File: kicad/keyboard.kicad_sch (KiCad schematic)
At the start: 64 parts

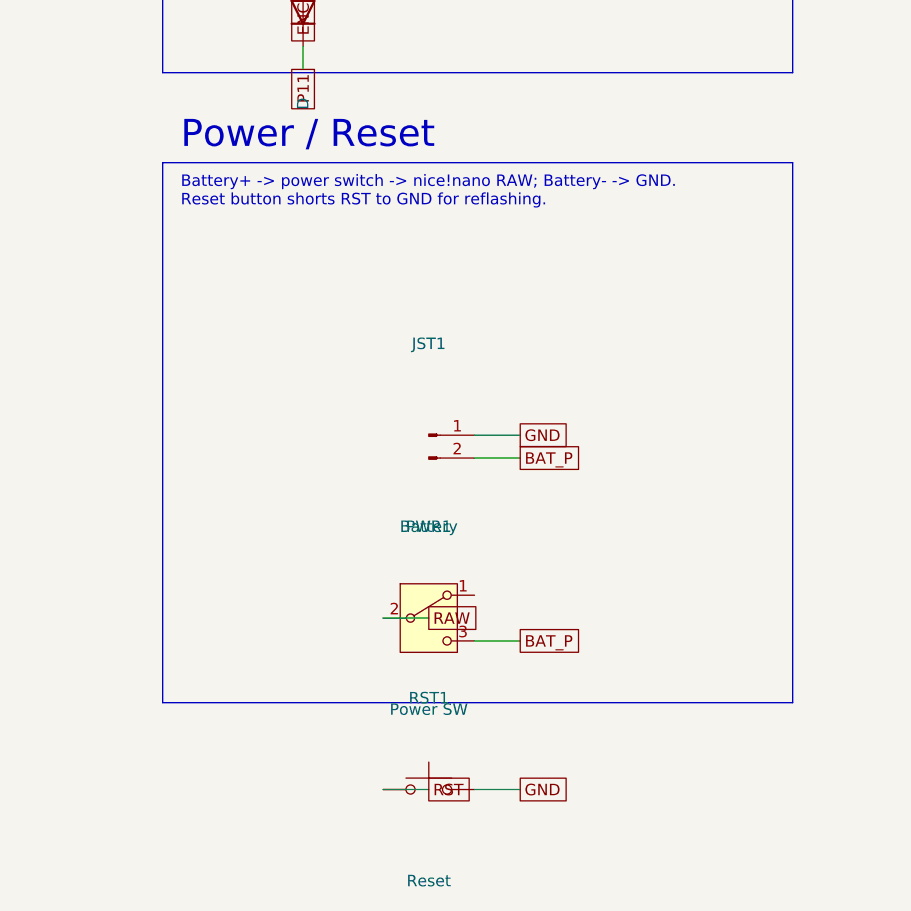
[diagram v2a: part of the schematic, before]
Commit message: Use Typeractive reset button (Panasonic EVQ-PUC02K, SMD side)
- Switch reset from reset_switch_tht_top to ceoloide/reset_switch_smd_side,
  which matches the Typeractive reset button (Panasonic EVQ-PUC02K). The
  power switch was already the matching part (Alps SSSS811101 =
  power_switch_smd_side), so it is unchanged.
- Vendor reset_switch_smd_side.js footprint
- Wiring verified: RST1 -> {GND, RST}; PWR1 -> {BAT_P, RAW}; matrix intact
- Schematic: map the new footprint, lay Power/Reset parts side-by-side so
  pin labels don't collide (fixes a schematic-only net short); netlist clean
- Regenerate output/ and KiCad project
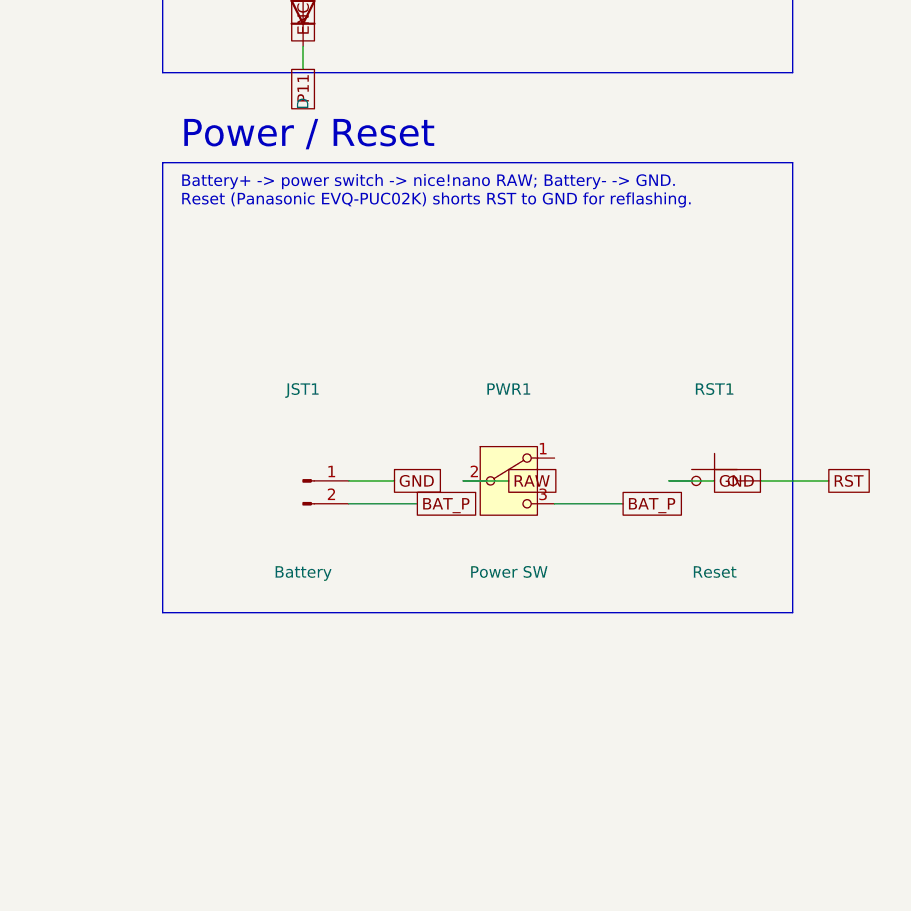
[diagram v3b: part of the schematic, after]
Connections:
- net GND: now also RST1.1; no longer RST1.2
- net RST: now also RST1.2; no longer RST1.1
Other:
- note added: "Battery+ -> power switch -> nice!nano RAW; Battery- -> GND. Reset (Panasonic EVQ-PUC02K) shorts RST to GND for reflashing."
- note removed: "Battery+ -> power switch -> nice!nano RAW; Battery- -> GND. Reset button shorts RST to GND for reflashing."
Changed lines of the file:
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@@
   (global_label "P11" (shape passive) (at 261.62 167.64 270)
     (effects (font (size 1.27 1.27)) (justify right)))
-  (rectangle (start 246.02 178.00) (end 316.02 238.00)
+  (rectangle (start 246.02 178.00) (end 316.02 228.00)
     (stroke (width 0.15) (type solid)) (fill (type none)))
   (text "Power / Reset" (at 248.02 175.00 0)
     (effects (font (size 3.0 3.0)) (justify left)))
-  (text "Battery+ -> power switch -> nice!nano RAW; Battery- -> GND.\nReset button shorts RST to GND for reflashing." (at 248.02 179.50 0)
+  (text "Battery+ -> power switch -> nice!nano RAW; Battery- -> GND.\nReset (Panasonic EVQ-PUC02K) shorts RST to GND for reflashing." (at 248.02 179.50 0)
     (effects (font (size 1.27 1.27)) (justify left top)))
-  (symbol (lib_id "Connector:Conn_01x02_Pin") (at 275.59 208.28 0) (unit 1)
+  (symbol (lib_id "Connector:Conn_01x02_Pin") (at 261.62 213.36 0) (unit 1)
     (in_bom yes) (on_board yes) (dnp no)
-    (property "Reference" "JST1" (at 275.59 198.12 0)
+    (property "Reference" "JST1" (at 261.62 203.20 0)
       (effects (font (size 1.27 1.27))))
-    (property "Value" "Battery" (at 275.59 218.44 0)
+    (property "Value" "Battery" (at 261.62 223.52 0)
       (effects (font (size 1.27 1.27))))
   )
-  (wire (pts (xy 280.67 208.28) (xy 285.75 208.28)) (stroke (width 0) (type default)))
-  (global_label "GND" (shape passive) (at 285.75 208.28 0)
+  (wire (pts (xy 266.70 213.36) (xy 271.78 213.36)) (stroke (width 0) (type default)))
+  (global_label "GND" (shape passive) (at 271.78 213.36 0)
     (effects (font (size 1.27 1.27)) (justify left)))
-  (wire (pts (xy 280.67 210.82) (xy 285.75 210.82)) (stroke (width 0) (type default)))
-  (global_label "BAT_P" (shape passive) (at 285.75 210.82 0)
+  (wire (pts (xy 266.70 215.90) (xy 274.32 215.90)) (stroke (width 0) (type default)))
+  (global_label "BAT_P" (shape passive) (at 274.32 215.90 0)
     (effects (font (size 1.27 1.27)) (justify left)))
-  (symbol (lib_id "Switch:SW_SPDT") (at 275.59 228.60 0) (unit 1)
+  (symbol (lib_id "Switch:SW_SPDT") (at 284.48 213.36 0) (unit 1)
     (in_bom yes) (on_board yes) (dnp no)
-    (property "Reference" "PWR1" (at 275.59 218.44 0)
+    (property "Reference" "PWR1" (at 284.48 203.20 0)
       (effects (font (size 1.27 1.27))))
-    (property "Value" "Power SW" (at 275.59 238.76 0)
+    (property "Value" "Power SW" (at 284.48 223.52 0)
       (effects (font (size 1.27 1.27))))
   )
-  (wire (pts (xy 270.51 228.60) (xy 275.59 228.60)) (stroke (width 0) (type default)))
-  (global_label "RAW" (shape passive) (at 275.59 228.60 0)
+  (wire (pts (xy 279.40 213.36) (xy 284.48 213.36)) (stroke (width 0) (type default)))
+  (global_label "RAW" (shape passive) (at 284.48 213.36 0)
     (effects (font (size 1.27 1.27)) (justify left)))
-  (wire (pts (xy 280.67 231.14) (xy 285.75 231.14)) (stroke (width 0) (type default)))
-  (global_label "BAT_P" (shape passive) (at 285.75 231.14 0)
+  (wire (pts (xy 289.56 215.90) (xy 297.18 215.90)) (stroke (width 0) (type default)))
+  (global_label "BAT_P" (shape passive) (at 297.18 215.90 0)
     (effects (font (size 1.27 1.27)) (justify left)))
-  (symbol (lib_id "Switch:SW_Push") (at 275.59 247.65 0) (unit 1)
+  (symbol (lib_id "Switch:SW_Push") (at 307.34 213.36 0) (unit 1)
     (in_bom yes) (on_board yes) (dnp no)
-    (property "Reference" "RST1" (at 275.59 237.49 0)
+    (property "Reference" "RST1" (at 307.34 203.20 0)
       (effects (font (size 1.27 1.27))))
-    (property "Value" "Reset" (at 275.59 257.81 0)
+    (property "Value" "Reset" (at 307.34 223.52 0)
       (effects (font (size 1.27 1.27))))
   )
-  (wire (pts (xy 280.67 247.65) (xy 285.75 247.65)) (stroke (width 0) (type default)))
-  (global_label "GND" (shape passive) (at 285.75 247.65 0)
+  (wire (pts (xy 302.26 213.36) (xy 307.34 213.36)) (stroke (width 0) (type default)))
+  (global_label "GND" (shape passive) (at 307.34 213.36 0)
     (effects (font (size 1.27 1.27)) (justify left)))
-  (wire (pts (xy 270.51 247.65) (xy 275.59 247.65)) (stroke (width 0) (type default)))
-  (global_label "RST" (shape passive) (at 275.59 247.65 0)
+  (wire (pts (xy 312.42 213.36) (xy 320.04 213.36)) (stroke (width 0) (type default)))
+  (global_label "RST" (shape passive) (at 320.04 213.36 0)
     (effects (font (size 1.27 1.27)) (justify left)))
   (sheet_instances (path "/" (page "1")))

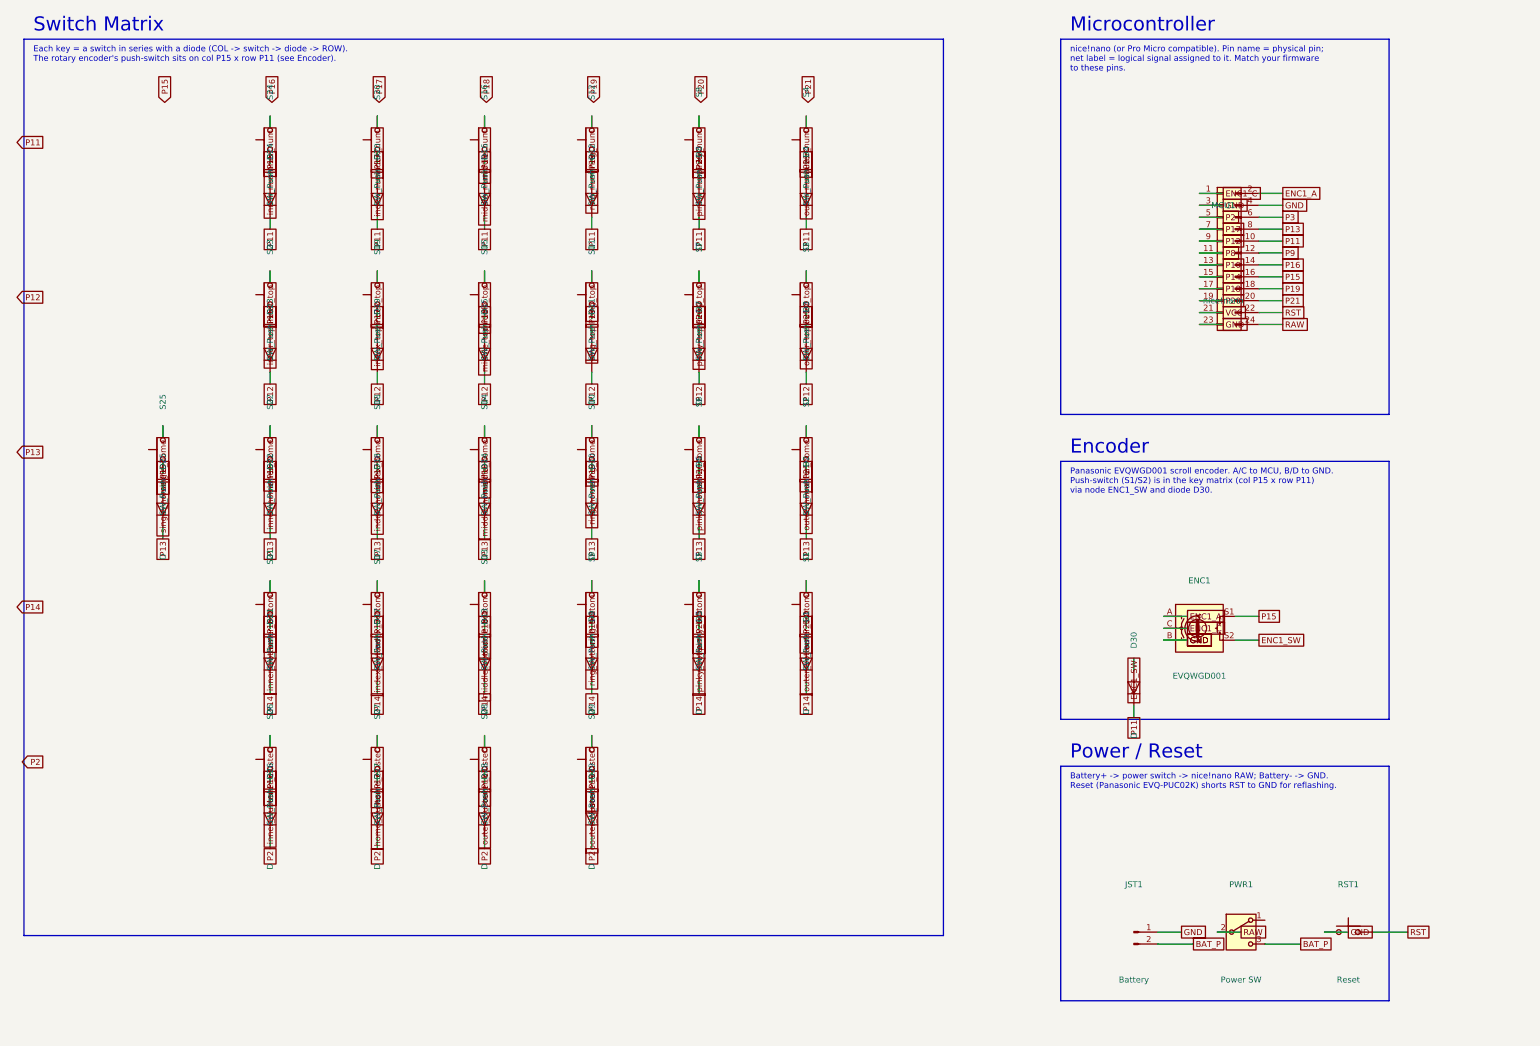
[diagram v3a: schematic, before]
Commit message: Draw matrix with real ROW bus wires (Lily58-style), labels only for COLs
Rework the switch matrix so connectivity uses drawn wire paths like the
reference schematic instead of per-pin labels everywhere:
- Horizontal ROW rails are real wires (one net each) with the ROW name
  labelled at the left endpoint; each diode cathode drops onto its row rail
  with a junction.
- Each switch's top pin gets a COL label (labels used only where the example
  uses them - column entry points).
- Fixed the root cause of earlier shorts: the ROW label must sit exactly on
  the rail's endpoint to attach; grid-align all matrix geometry so pin taps
  land precisely on wires/rails.
Netlist verified fully correct (54 nets): columns=switches+MCU, rows=diodes+
MCU, encoder/power/reset all isolated. ERC only cosmetic warnings.
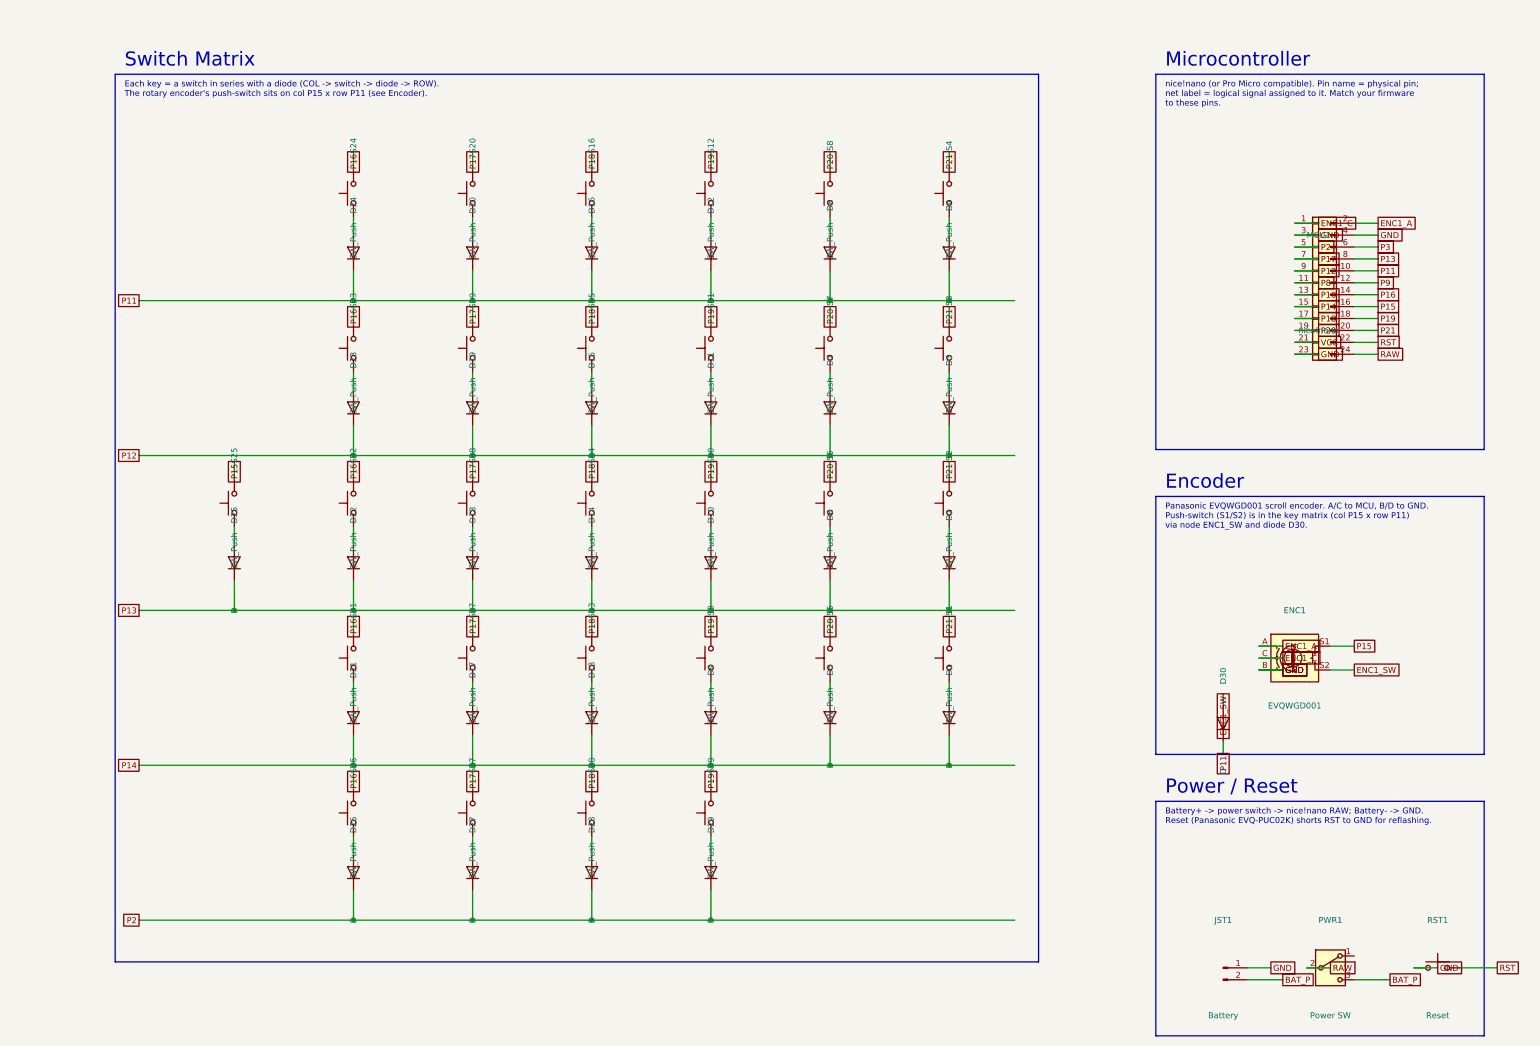
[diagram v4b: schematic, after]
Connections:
- net P15: now also S25.2; no longer S25.1
- net P16: now also S21.2, S22.2, S23.2, S24.2, S26.2; no longer S21.1, S22.1, S23.1, S24.1, S26.1
- net P17: now also S17.2, S18.2, S19.2, S20.2, S27.2; no longer S17.1, S18.1, S19.1, S20.1, S27.1
- net P18: now also S13.2, S14.2, S15.2, S16.2, S28.2; no longer S13.1, S14.1, S15.1, S16.1, S28.1
- net P19: now also S10.2, S11.2, S12.2, S29.2, S9.2; no longer S10.1, S11.1, S12.1, S29.1, S9.1
- net P20: now also S5.2, S6.2, S7.2, S8.2; no longer S5.1, S6.1, S7.1, S8.1
- net P21: now also S1.2, S2.2, S3.2, S4.2; no longer S1.1, S2.1, S3.1, S4.1
- net home_cluster: no longer names the net of D27.2 (A)
- net home_cluster: now also S27.1; no longer S27.2
- net index_bottom: no longer names the net of D17.2 (A)
- net index_bottom: now also S17.1; no longer S17.2
- net index_home: no longer names the net of D18.2 (A)
- net index_home: now also S18.1; no longer S18.2
- net index_num: no longer names the net of D20.2 (A)
- net index_num: now also S20.1; no longer S20.2
- net index_top: no longer names the net of D19.2 (A)
- net index_top: now also S19.1; no longer S19.2
- net inner_bottom: no longer names the net of D21.2 (A)
- net inner_bottom: now also S21.1; no longer S21.2
- net inner_cluster: no longer names the net of D26.2 (A)
- net inner_cluster: now also S26.1; no longer S26.2
- net inner_home: no longer names the net of D22.2 (A)
- net inner_home: now also S22.1; no longer S22.2
- net inner_num: no longer names the net of D24.2 (A)
- net inner_num: now also S24.1; no longer S24.2
- net inner_top: no longer names the net of D23.2 (A)
- net inner_top: now also S23.1; no longer S23.2
- net middle_bottom: no longer names the net of D13.2 (A)
- net middle_bottom: now also S13.1; no longer S13.2
- net middle_home: no longer names the net of D14.2 (A)
- net middle_home: now also S14.1; no longer S14.2
- net middle_num: no longer names the net of D16.2 (A)
- net middle_num: now also S16.1; no longer S16.2
- net middle_top: no longer names the net of D15.2 (A)
- net middle_top: now also S15.1; no longer S15.2
- net oouter_cluster: no longer names the net of D29.2 (A)
- net oouter_cluster: now also S29.1; no longer S29.2
- net outer_bottom: no longer names the net of D1.2 (A)
- net outer_bottom: now also S1.1; no longer S1.2
- net outer_cluster: no longer names the net of D28.2 (A)
- net outer_cluster: now also S28.1; no longer S28.2
- net outer_home: no longer names the net of D2.2 (A)
- net outer_home: now also S2.1; no longer S2.2
- net outer_num: no longer names the net of D4.2 (A)
- net outer_num: now also S4.1; no longer S4.2
- net outer_top: no longer names the net of D3.2 (A)
- net outer_top: now also S3.1; no longer S3.2
- net pinky_bottom: no longer names the net of D5.2 (A)
- net pinky_bottom: now also S5.1; no longer S5.2
- net pinky_home: no longer names the net of D6.2 (A)
- net pinky_home: now also S6.1; no longer S6.2
- net pinky_num: no longer names the net of D8.2 (A)
- net pinky_num: now also S8.1; no longer S8.2
- net pinky_top: no longer names the net of D7.2 (A)
- net pinky_top: now also S7.1; no longer S7.2
- net ring_bottom: no longer names the net of D9.2 (A)
- net ring_bottom: now also S9.1; no longer S9.2
- net ring_home: no longer names the net of D10.2 (A)
- net ring_home: now also S10.1; no longer S10.2
- net ring_num: no longer names the net of D12.2 (A)
- net ring_num: now also S12.1; no longer S12.2
- net ring_top: no longer names the net of D11.2 (A)
- net ring_top: now also S11.1; no longer S11.2
- net single_home: no longer names the net of D25.2 (A)
- net single_home: now also S25.1; no longer S25.2
